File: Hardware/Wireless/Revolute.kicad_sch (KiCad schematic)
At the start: 54 parts, among them Q2 AO3407, U1 BQ27441-G1, U2 Button, U2 nrf52833_qfn40, U3 AS5600, U3 MAX16054, U4 AP2112K-3.3, U5 BQ24075RGT, X1 32.768 kHz, X2 32MHZ

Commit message: worked on wireless
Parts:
- removed Q2: AO3407, Package_TO_SOT_SMD:SOT-23, symbol nrfmicro-rescue:BSS83P
- removed R2: 5.1K, Resistor_SMD:R_0402_1005Metric, symbol Device:R
- removed U3: MAX16054, Package_TO_SOT_SMD:SOT-23-6, symbol Library:MAX16054
- added U41: ~, Library:BK13C06-10DS, symbol Library:BK13C06-10D(S/P)
- added U41: ~, Library:BK13C06-10DP, symbol Library:BK13C06-10D(S/P)
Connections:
- net vSYSTEM is gone; now on net OUT: C22.1, C26.1, U4.1 (VIN), U4.3 (EN)
- net D+: now also U41.9 (NFC1)
- net D-: now also U41.10 (NFC2)
- net GND: now also U41.1 (VDD), U41.14 (VCC), U41.15 (VCC), U41.16 (VCC), U41.5 (SCL)
- net P0.15: now also U41.6 (B1)
- net P0.17: now also U41.7 (B2)
- net RESET: now also U41.4 (SDA)
- net VDD_nRF: now also U41.11 (GND), U41.12 (GND), U41.13 (GND), U41.8 (APDS_IRQ)
- net swc: now also U41.2 (PDM_DAT)
- net swd: now also U41.3 (PDM_CLK)
- net at U2.3: now also U2.33 (P0.28/AIN4)
- no-connect marks 3 -> 0
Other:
- moved on the sheet: U2

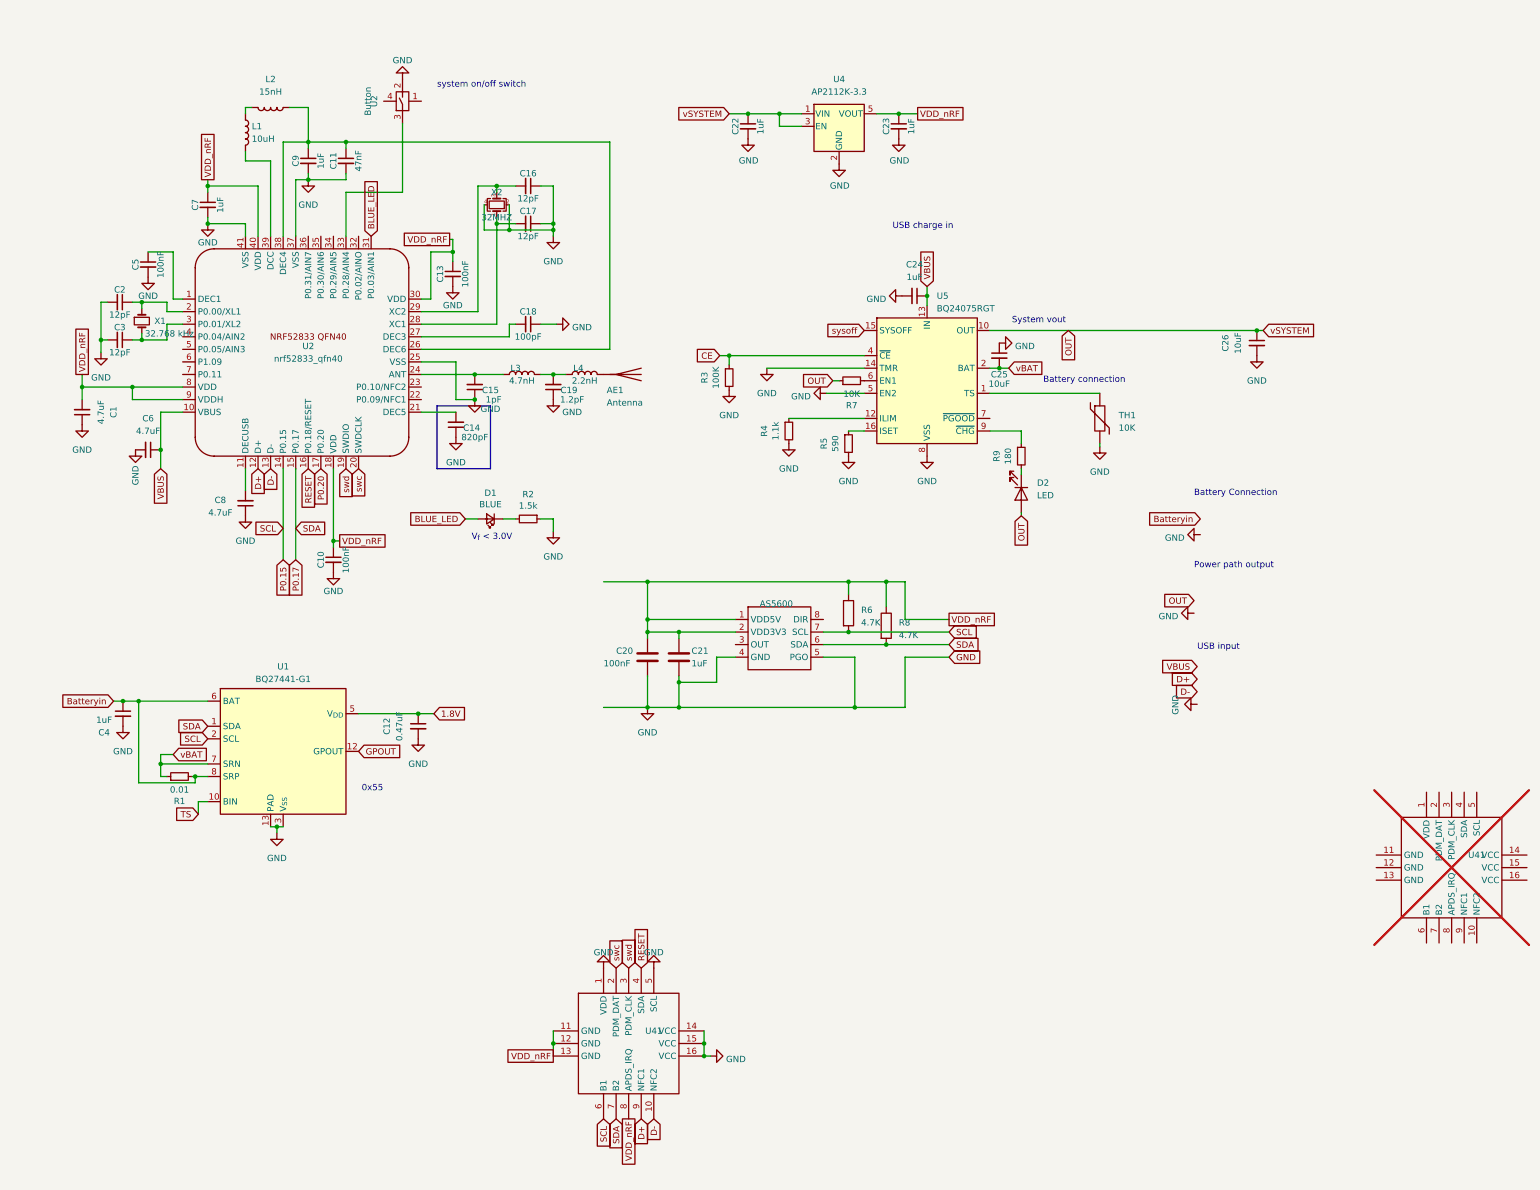
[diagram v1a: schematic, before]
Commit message: added debug board (work in progress)
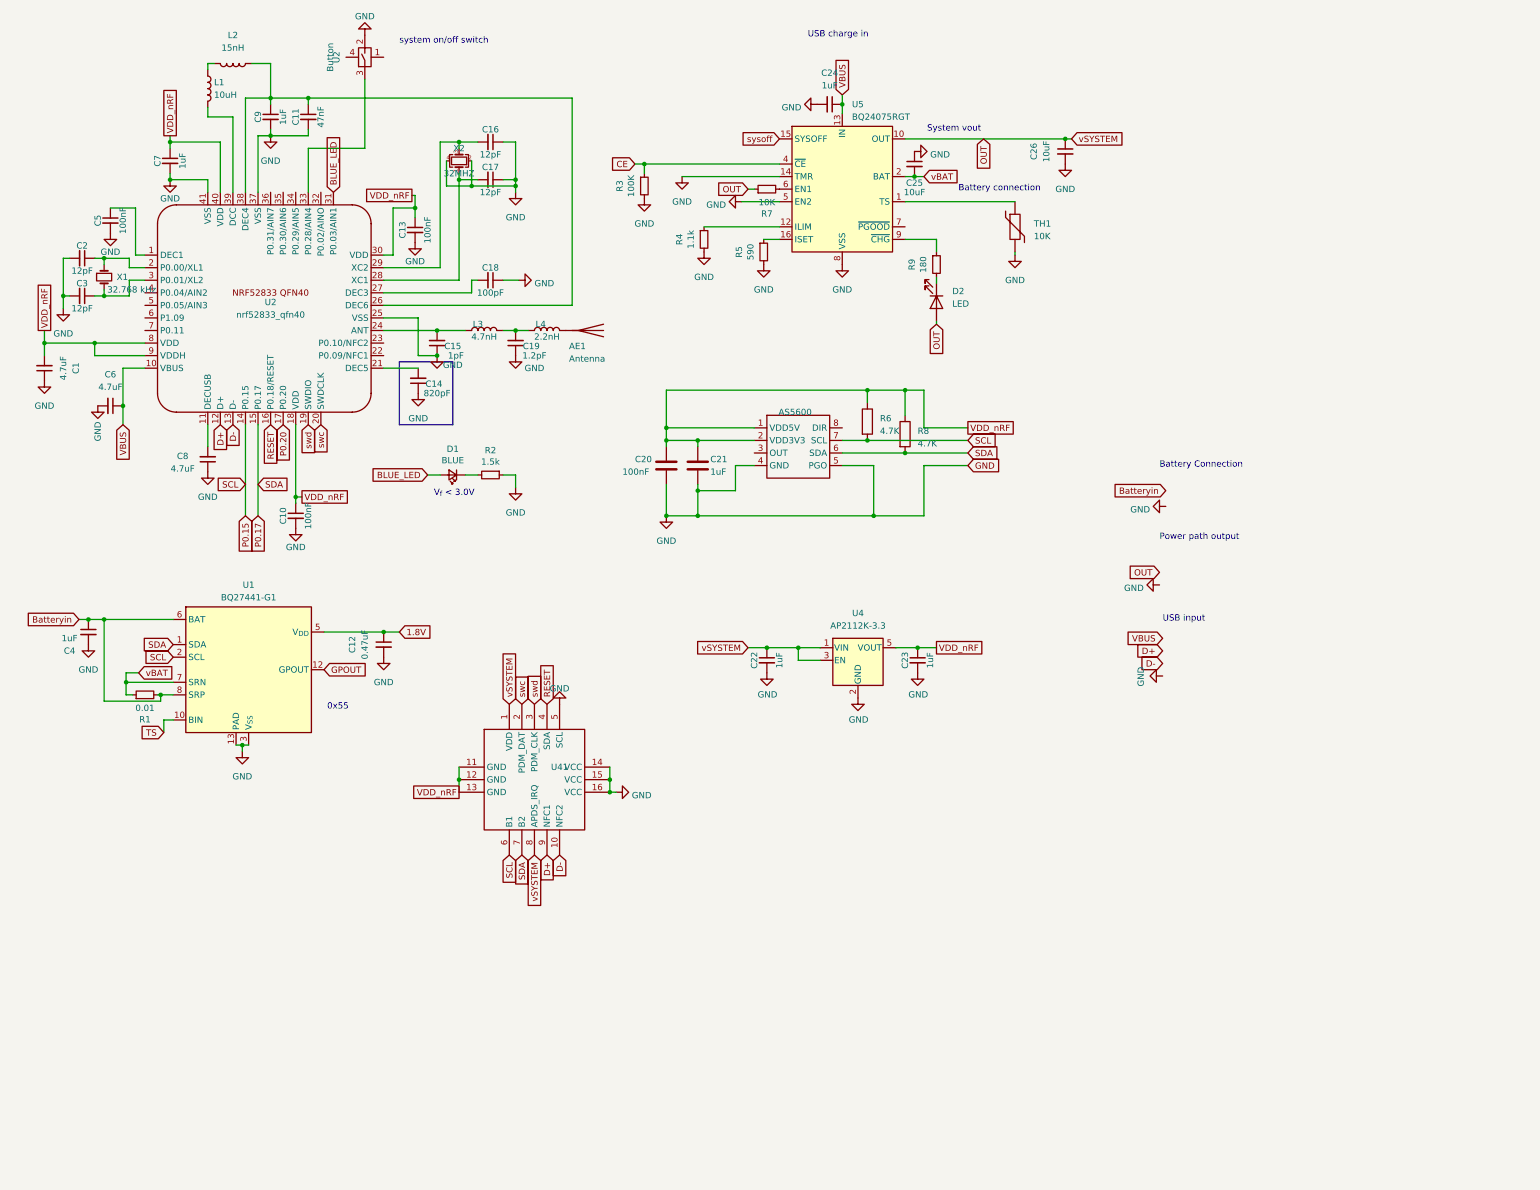
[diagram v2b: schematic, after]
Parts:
- removed U41: ~, Library:BK13C06-10DS, symbol Library:BK13C06-10D(S/P)
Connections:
- net GND: no longer U41.1 (VDD)
- net OUT: now also U41.1 (VDD), U41.8 (APDS_IRQ)
- net VDD_nRF: no longer U41.8 (APDS_IRQ)
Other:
- moved on the sheet: AE1, C1, C10, C11, C12, C13, C14, C15, C16, C17, C18, C19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

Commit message: fixed design
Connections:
- net OUT: no longer U41.1 (VDD), U41.8 (APDS_IRQ)
- net VBUS: now also U41.1 (VDD), U41.8 (APDS_IRQ)
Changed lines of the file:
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@@
-    )
-  )
-  (global_label "vSYSTEM" (shape input) (at 115.57 151.765 90) (fields_autoplaced)
-    (effects (font (size 1.27 1.27)) (justify left))
-    (property "Intersheetrefs" "${INTERSHEET_REFS}" (at 115.57 140.816 90)
-      (effects (font (size 1.27 1.27)) (justify left) hide)
     )
   )
@@
     )
   )
+  (global_label "VBUS" (shape input) (at 115.57 151.765 90) (fields_autoplaced)
+    (effects (font (size 1.27 1.27)) (justify left))
+    (property "Intersheetrefs" "${INTERSHEET_REFS}" (at 115.57 143.9606 90)
+      (effects (font (size 1.27 1.27)) (justify left) hide)
+    )
+  )
   (global_label "swc" (shape input) (at 118.11 151.765 90) (fields_autoplaced)
     (effects (font (size 1.27 1.27)) (justify left))
@@
     )
   )
+  (global_label "VBUS" (shape input) (at 120.65 182.245 270) (fields_autoplaced)
+    (effects (font (size 1.27 1.27)) (justify right))
+    (property "Intersheetrefs" "${INTERSHEET_REFS}" (at 120.65 190.0494 90)
+      (effects (font (size 1.27 1.27)) (justify right) hide)
+    )
+  )
   (global_label "OUT" (shape input) (at 211.455 37.465 270) (fields_autoplaced)
     (effects (font (size 1.27 1.27)) (justify right))
@@
     )
   )
-  (global_label "vSYSTEM" (shape input) (at 120.65 182.245 270) (fields_autoplaced)
-    (effects (font (size 1.27 1.27)) (justify right))
-    (property "Intersheetrefs" "${INTERSHEET_REFS}" (at 120.65 193.194 90)
-      (effects (font (size 1.27 1.27)) (justify right) hide)
-    )
-  )

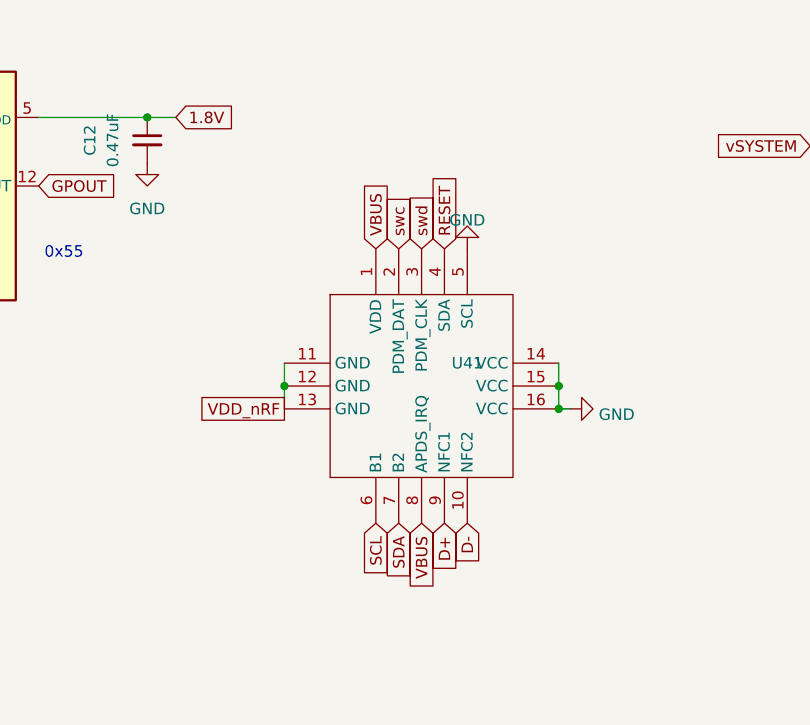
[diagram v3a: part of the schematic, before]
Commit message: added pogo charging pins, fixed debug connector
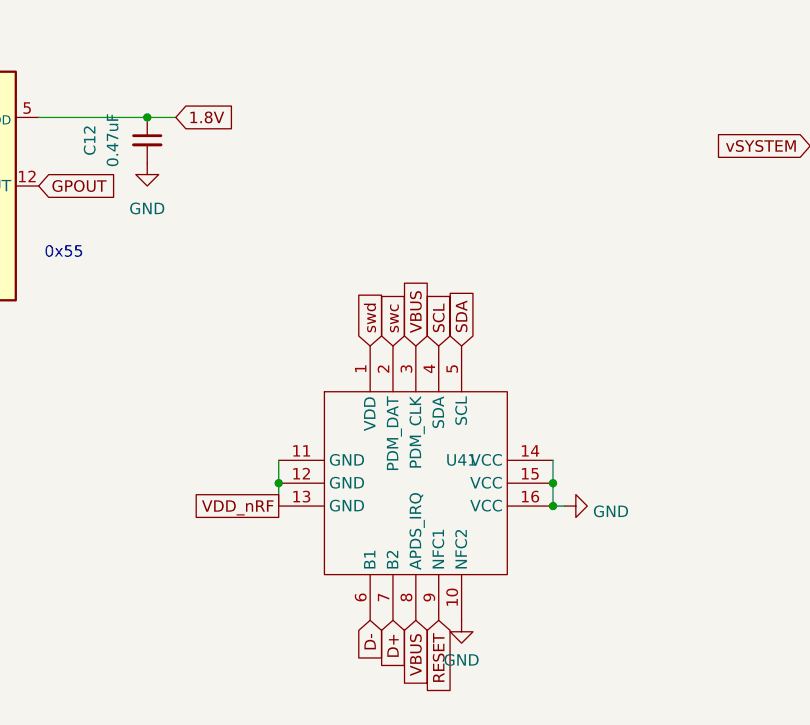
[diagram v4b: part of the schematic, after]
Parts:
- U41: footprint Library:BK13C06-10DP -> Library:BK13C06-10DS
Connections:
- net D+: now also U41.7 (B2); no longer U41.9 (NFC1)
- net D-: now also U41.6 (B1); no longer U41.10 (NFC2)
- net GND: now also U41.10 (NFC2); no longer U41.5 (SCL)
- net P0.15: now also U41.4 (SDA); no longer U41.6 (B1)
- net P0.17: now also U41.5 (SCL); no longer U41.7 (B2)
- net RESET: now also U41.9 (NFC1); no longer U41.4 (SDA)
- net VBUS: now also U41.3 (PDM_CLK); no longer U41.1 (VDD)
- net swd: now also U41.1 (VDD); no longer U41.3 (PDM_CLK)

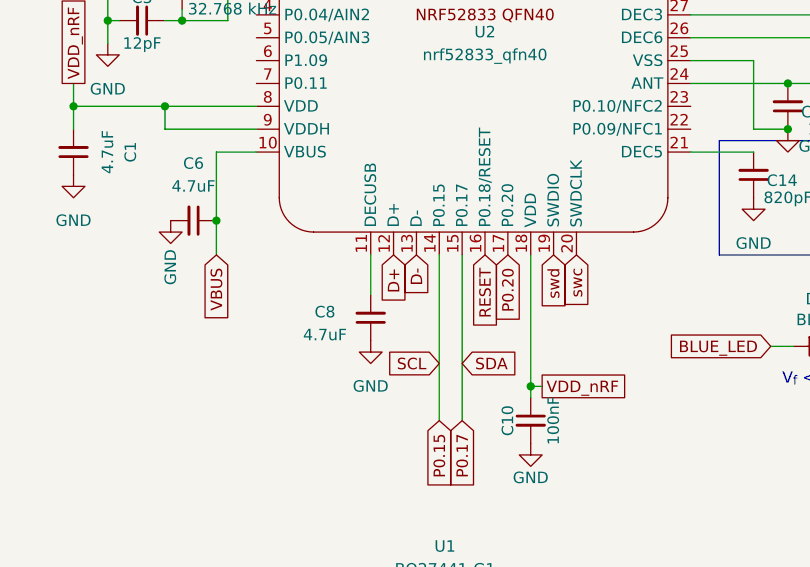
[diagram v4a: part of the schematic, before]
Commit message: fixed usb datapin issue
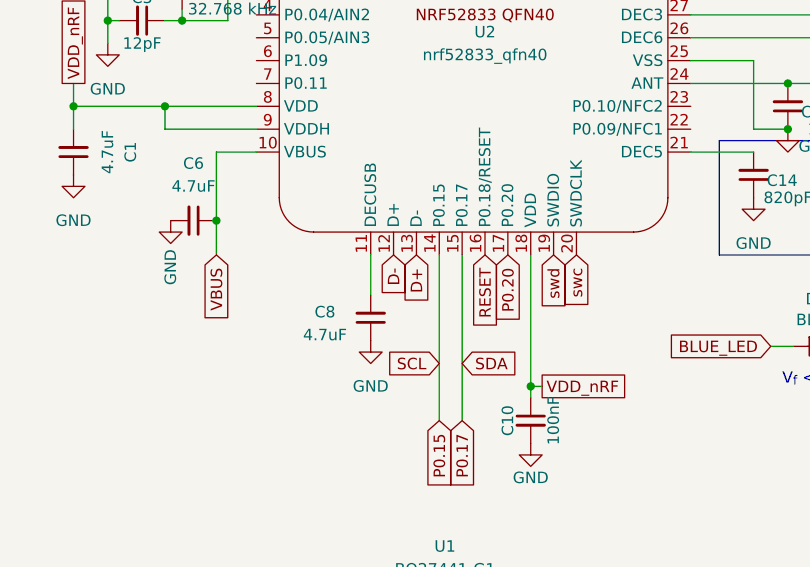
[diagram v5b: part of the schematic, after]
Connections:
- net D+: now also U2.13 (D-); no longer U2.12 (D+)
- net D-: now also U2.12 (D+); no longer U2.13 (D-)
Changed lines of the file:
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@@
     )
   )
-  (global_label "D-" (shape input) (at 59.69 95.25 270) (fields_autoplaced)
+  (global_label "D-" (shape input) (at 57.15 95.25 270) (fields_autoplaced)
     (effects (font (size 1.27 1.27)) (justify right))
-    (property "Intersheetrefs" "${INTERSHEET_REFS}" (at 59.69 100.9982 90)
+    (property "Intersheetrefs" "${INTERSHEET_REFS}" (at 57.15 100.9982 90)
       (effects (font (size 1.27 1.27)) (justify right) hide)
     )
@@
     )
   )
-  (global_label "D+" (shape input) (at 57.15 95.25 270) (fields_autoplaced)
+  (global_label "D+" (shape input) (at 59.69 95.25 270) (fields_autoplaced)
     (effects (font (size 1.27 1.27)) (justify right))
-    (property "Intersheetrefs" "${INTERSHEET_REFS}" (at 57.15 100.9982 90)
+    (property "Intersheetrefs" "${INTERSHEET_REFS}" (at 59.69 100.9982 90)
       (effects (font (size 1.27 1.27)) (justify right) hide)
     )

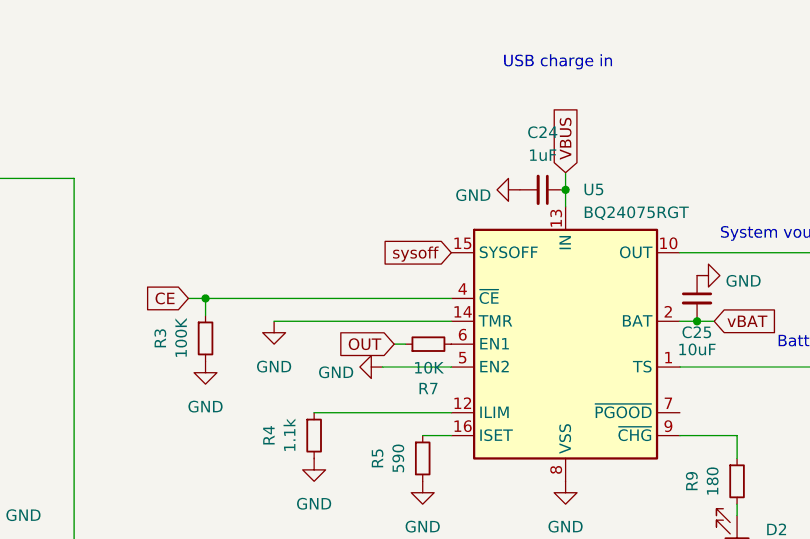
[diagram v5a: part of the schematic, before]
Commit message: worked on software, fixed wireless pcb power path circuit
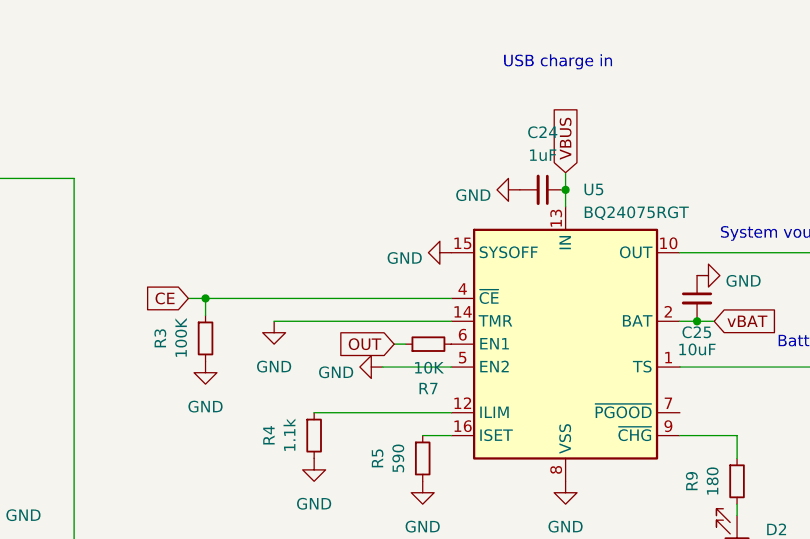
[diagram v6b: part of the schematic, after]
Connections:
- net sysoff is gone; now on net GND: U5.15 (SYSOFF)
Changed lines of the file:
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@@
-    )
-  )
-  (global_label "sysoff" (shape input) (at 170.18 37.465 180) (fields_autoplaced)
-    (effects (font (size 1.27 1.27)) (justify right))
-    (property "Intersheetrefs" "${INTERSHEET_REFS}" (at 161.65 37.465 0)
-      (effects (font (size 1.27 1.27)) (justify right) hide)
     )
   )
@@
         )
       )
+    )
+  )
+  (symbol (lib_id "power:GND") (at 170.18 37.465 270) (unit 1)
+    (in_bom yes) (on_board yes) (dnp no) (fields_autoplaced)
+    (property "Reference" "#PWR039" (at 163.83 37.465 0)
+      (effects (font (size 1.27 1.27)) hide)
+    )
+    (property "Value" "GND" (at 167.005 38.1 90)
+      (effects (font (size 1.27 1.27)) (justify right))
+    )
+    (property "Footprint" "" (at 170.18 37.465 0)
+      (effects (font (size 1.27 1.27)) hide)
+    )
+    (property "Datasheet" "" (at 170.18 37.465 0)
+      (effects (font (size 1.27 1.27)) hide)
+    )
+    (pin "1")
+    (instances
+      (project "Revolute"
+        (path "/e63e39d7-6ac0-4ffd-8aa3-1841a4541b55"
+          (reference "#PWR039") (unit 1)
+        )
+      )
